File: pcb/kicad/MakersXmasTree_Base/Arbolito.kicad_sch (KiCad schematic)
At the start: 54 parts, among them J1 Battery, J2 Header 1x06 2.54mm, P1 USB_C_Plug_USB2.0, Q1 S8050, Q2 S8050, SW1 SW_DPDT_x2, SW2 SW_Push, SW3 SW_Push, SW4 SW_Push, U1 NCP115AMX120TCG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

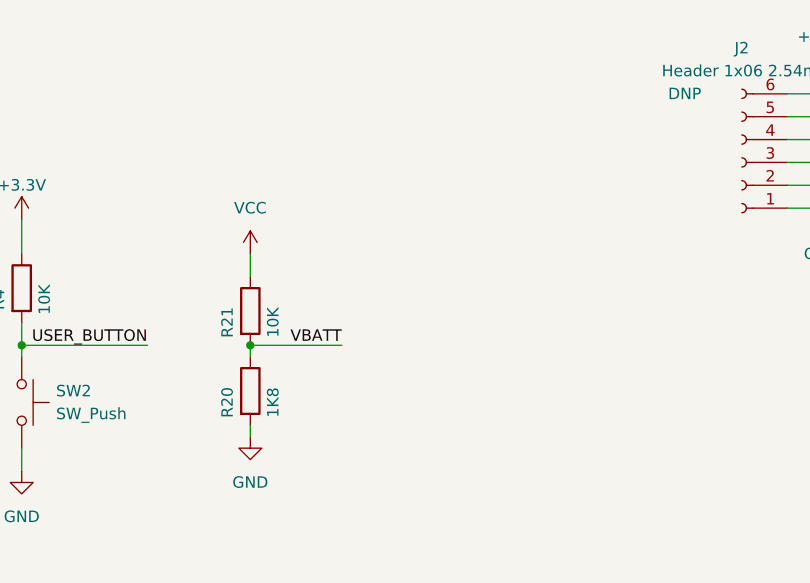
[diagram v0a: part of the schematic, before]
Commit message: Change R20 with 1K resistor
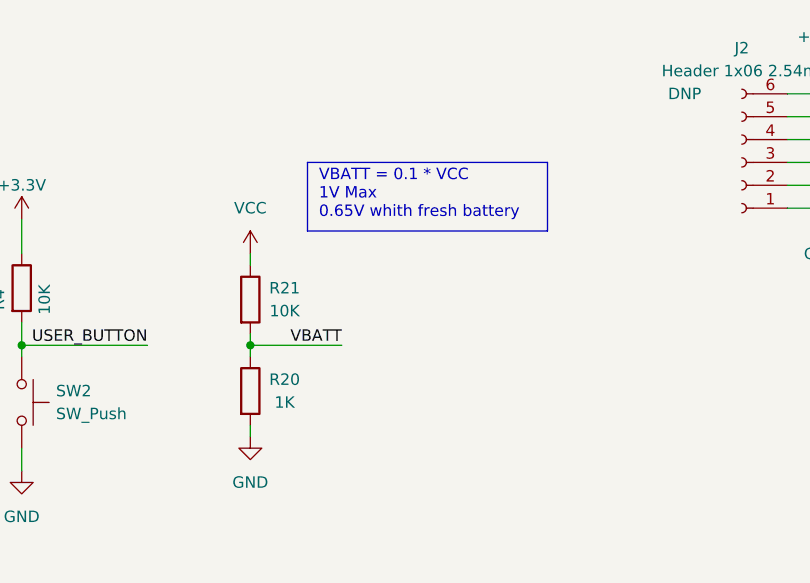
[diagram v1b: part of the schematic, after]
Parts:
- R20: value 1K8 -> 1K
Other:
- note added: "VBATT = 0.1 * VCC 1V Max 0.65V whith fresh battery"
- moved on the sheet: R21
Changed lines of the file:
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@@
+    (stroke (width 0) (type default) (color 0 0 0 0))
+  )
+  (polyline (pts (xy 175.26 157.48) (xy 148.59 157.48))
+    (stroke (width 0) (type default) (color 0 0 0 0))
+  )
+  (polyline (pts (xy 148.59 149.86) (xy 148.59 157.48))
     (stroke (width 0) (type default) (color 0 0 0 0))
   )
@@
     (stroke (width 0) (type default) (color 0 0 0 0))
   )
+  (polyline (pts (xy 148.59 149.86) (xy 175.26 149.86))
+    (stroke (width 0) (type default) (color 0 0 0 0))
+  )
   (wire (pts (xy 44.45 33.02) (xy 48.26 33.02))
     (stroke (width 0) (type default) (color 0 0 0 0))
@@
     (stroke (width 0) (type default) (color 0 0 0 0))
   )
+  (polyline (pts (xy 175.26 149.86) (xy 175.26 157.48))
+    (stroke (width 0) (type default) (color 0 0 0 0))
+  )
   (wire (pts (xy 105.41 73.66) (xy 129.54 73.66))
     (stroke (width 0) (type default) (color 0 0 0 0))
@@
   )
   (wire (pts (xy 60.96 20.32) (xy 60.96 29.21))
+    (stroke (width 0) (type default) (color 0 0 0 0))
+  )
+  (wire (pts (xy 142.24 168.91) (xy 142.24 170.18))
     (stroke (width 0) (type default) (color 0 0 0 0))
   )
@@
     (stroke (width 0) (type default) (color 0 0 0 0))
   )
-  (wire (pts (xy 142.24 160.02) (xy 142.24 162.56))
+  (wire (pts (xy 142.24 160.02) (xy 142.24 161.29))
     (stroke (width 0) (type default) (color 0 0 0 0))
   )
@@
   (wire (pts (xy 116.84 170.18) (xy 116.84 167.64))
     (stroke (width 0) (type default) (color 0 0 0 0))
+  )
+  (text "VBATT = 0.1 * VCC\n1V Max\n0.65V whith fresh battery"
+    (at 149.86 156.21 0)
+    (effects (font (size 1.27 1.27)) (justify left bottom))
   )
   (label "D+" (at 53.34 88.9 0)
@@
   (symbol (lib_id "Device:R") (at 142.24 175.26 0) (unit 1)
     (in_bom yes) (on_board yes)
-    (property "Reference" "R20" (id 0) (at 139.7 176.53 90))
-    (property "Value" "1K8" (id 1) (at 144.78 176.53 90))
+    (property "Reference" "R20" (id 0) (at 146.05 173.99 0))
+    (property "Value" "1K" (id 1) (at 146.05 176.53 0))
     (property "Footprint" "Resistor_SMD:R_0805_2012Metric_Pad1.20x1.40mm_HandSolder" (id 2) (at 140.462 175.26 90)
       (effects (font (size 1.27 1.27)) hide)
@@
     (pin "1")
   )
-  (symbol (lib_id "Device:R") (at 142.24 166.37 0) (unit 1)
-    (in_bom yes) (on_board yes)
-    (property "Reference" "R21" (id 0) (at 139.7 167.64 90))
-    (property "Value" "10K" (id 1) (at 144.78 167.64 90))
-    (property "Footprint" "Resistor_SMD:R_0805_2012Metric_Pad1.20x1.40mm_HandSolder" (id 2) (at 140.462 166.37 90)
-      (effects (font (size 1.27 1.27)) hide)
-    )
-    (property "Datasheet" "~" (id 3) (at 142.24 166.37 0)
+  (symbol (lib_id "Device:R") (at 142.24 165.1 0) (unit 1)
+    (in_bom yes) (on_board yes)
+    (property "Reference" "R21" (id 0) (at 146.05 163.83 0))
+    (property "Value" "10K" (id 1) (at 146.05 166.37 0))
+    (property "Footprint" "Resistor_SMD:R_0805_2012Metric_Pad1.20x1.40mm_HandSolder" (id 2) (at 140.462 165.1 90)
+      (effects (font (size 1.27 1.27)) hide)
+    )
+    (property "Datasheet" "~" (id 3) (at 142.24 165.1 0)
       (effects (font (size 1.27 1.27)) hide)
     )
@@
     )
     (path "/68865ec2-ae21-4231-80be-99081fdc9d3a"
-      (reference "R20") (unit 1) (value "1K8") (footprint "Resistor_SMD:R_0805_2012Metric_Pad1.20x1.40mm_HandSolder")
+      (reference "R20") (unit 1) (value "1K") (footprint "Resistor_SMD:R_0805_2012Metric_Pad1.20x1.40mm_HandSolder")
     )
     (path "/b8e3cfcf-9b64-4364-9810-244bcf8c4f91"
